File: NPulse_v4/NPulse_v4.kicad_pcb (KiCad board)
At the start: 4 copper layers, 39.8 x 72.5 mm, 163 parts, among them IC1 TXU0202QDCUR, IC2 DRV8220DSGR, IC3 DRV8220DSGR, IC4 DRV8220DSGR, IC5 DRV8220DSGR, IC6 DRV8220DSGR, IC7 DRV8220DSGR, IC8 DRV8220DSGR, IC9 DRV8220DSGR, J11 Conn_02x05_Odd_Even, J2 Conn_01x04_Pin, J3 Conn_01x06_Pin, J4 Conn_01x04_Pin, J5 Conn_02x05_Odd_Even, J6 Conn_02x05_Odd_Even, J7 Conn_02x05_Odd_Even, J8 Conn_02x05_Odd_Even, J9 Conn_02x05_Odd_Even, Q1 PMOS, Q2 NMOS, SW1 SW_Push, SW2 SW_SPDT, U1 STM32G484METx, U11 TPS7A0533PDBZ, U2 SN74LVC002, U3 SN74LVC002, U4 SN74LVC002, U5 SN74LVC002, U6 SN74LVC002, U7 SN74LVC002, U8 SN74LVC002, U9 SN74LVC002, Y1 16MHz

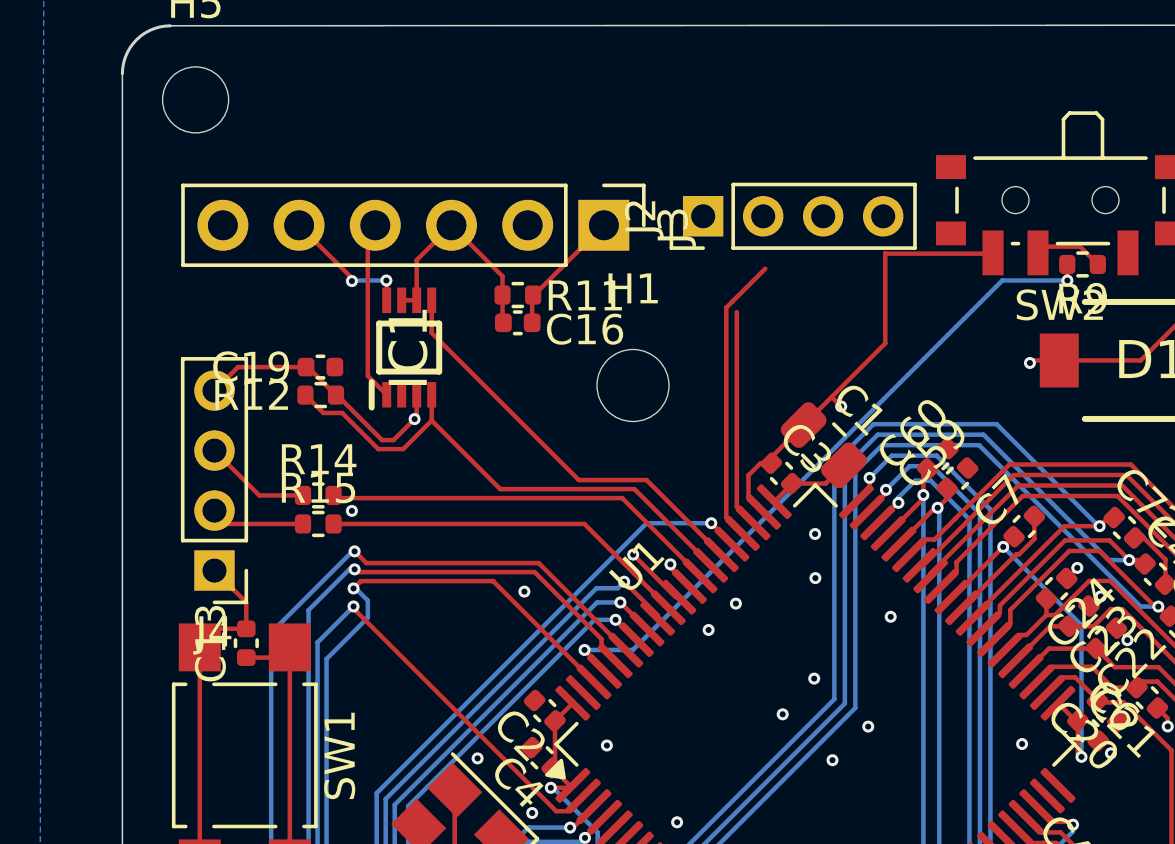
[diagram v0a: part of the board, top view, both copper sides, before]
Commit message: Replace vias and change connectors footprint on control board
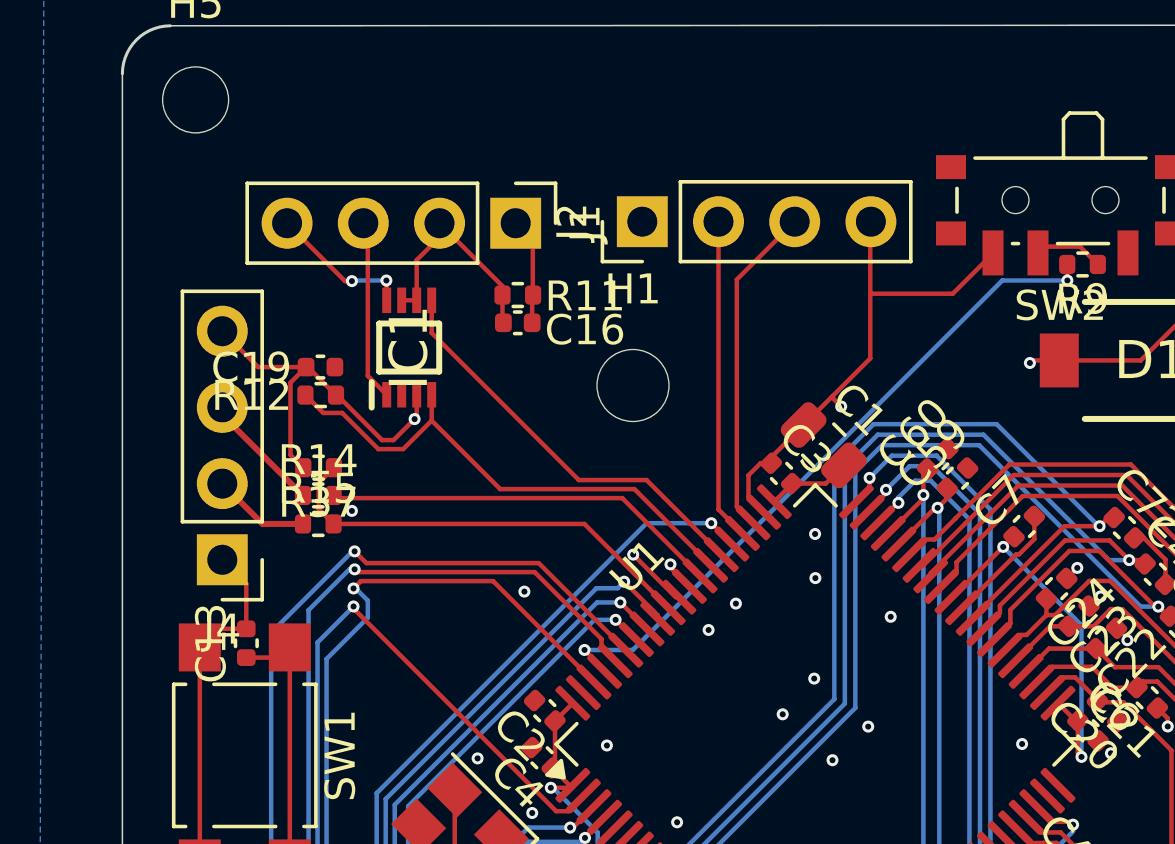
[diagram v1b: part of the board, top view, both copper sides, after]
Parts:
- removed J3: Conn_01x06_Pin, Connector_PinHeader_2.54mm:PinHeader_1x06_P2.54mm_Vertical
- added J1: USB-to-UART, Connector_PinHeader_2.54mm:PinHeader_1x04_P2.54mm_Vertical, F.Cu at (166.5, 71.8)
- added R37: 100k, Resistor_SMD:R_0402_1005Metric, F.Cu at (159.9, 79.9)
- J2, J4: footprint Connector_PinHeader_2.00mm:PinHeader_1x04_P2.00mm_Vertical -> Connector_PinHeader_2.54mm:PinHeader_1x04_P2.54mm_Vertical
- moved J2 2.04 mm to (170.7, 71.7)
- moved J4 0.44 mm to (156.7, 83.0)
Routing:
- net +3.3V: track 197.5 -> 203.1 mm
- net /SWDIO: track 7.25 -> 11.1 mm
- net EMG_RX: track 12.3 -> 14.6 mm
- net /SWCLK: track 9.59 -> 10.7 mm

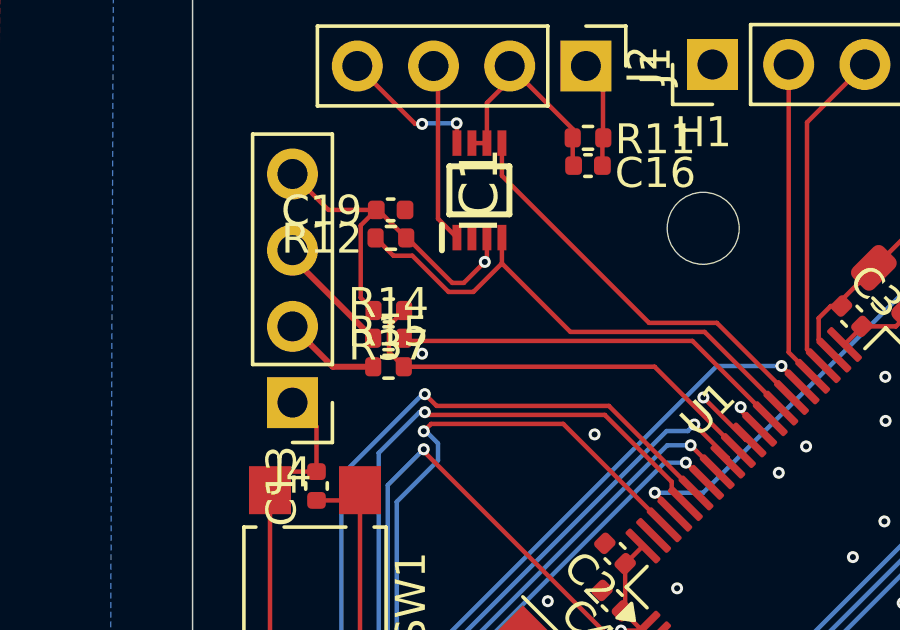
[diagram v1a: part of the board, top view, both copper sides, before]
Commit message: restructure files and change vias on hat to 0.45mm diam
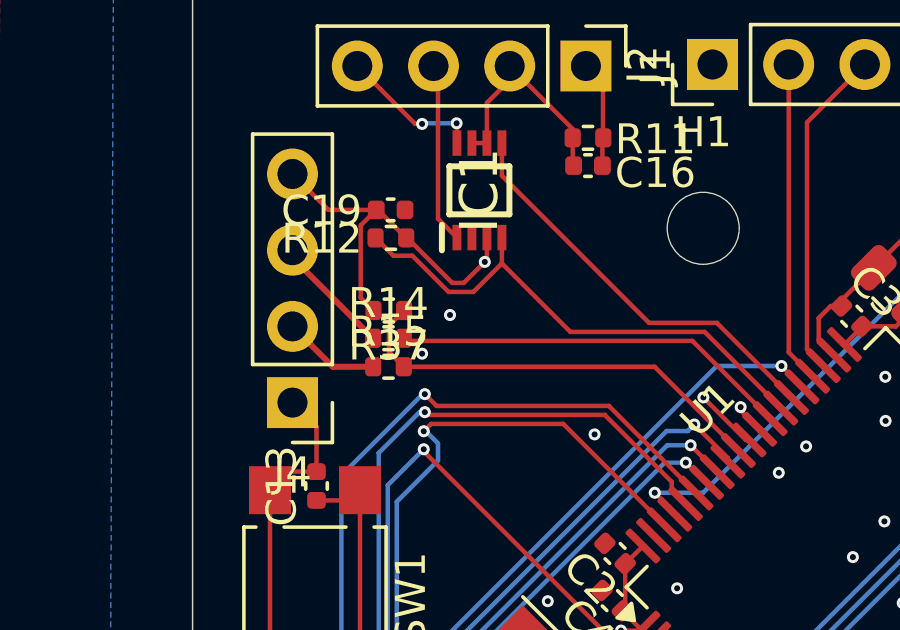
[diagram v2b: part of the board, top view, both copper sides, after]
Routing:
- net GND: vias 93 -> 94
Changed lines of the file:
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@@
 			(outputformat 1)
 			(mirror no)
-			(drillshape 1)
+			(drillshape 0)
 			(scaleselection 1)
-			(outputdirectory "")
+			(outputdirectory "gerbers_ctrl/")
 		)
 	)
@@
 		(size 0.4)
 		(drill 0.2)
+		(layers "F.Cu" "B.Cu")
+		(free yes)
+		(net 2)
+	)
+	(via
+		(at 161.95 80.05)
+		(size 0.4)
+		(drill 0.2)
